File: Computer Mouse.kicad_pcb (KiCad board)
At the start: 2 copper layers, 86 parts, among them J1 Conn_01x05, J2 USB_C_Receptacle_USB2.0, J3 Conn_01x02, SW1 SW_SPST, SW2 SW_SPDT, SW3 SW_SPDT, SW4 RotaryEncoder, SW5 SW_SPDT, SW6 SW_SPDT, SW7 RotaryEncoder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

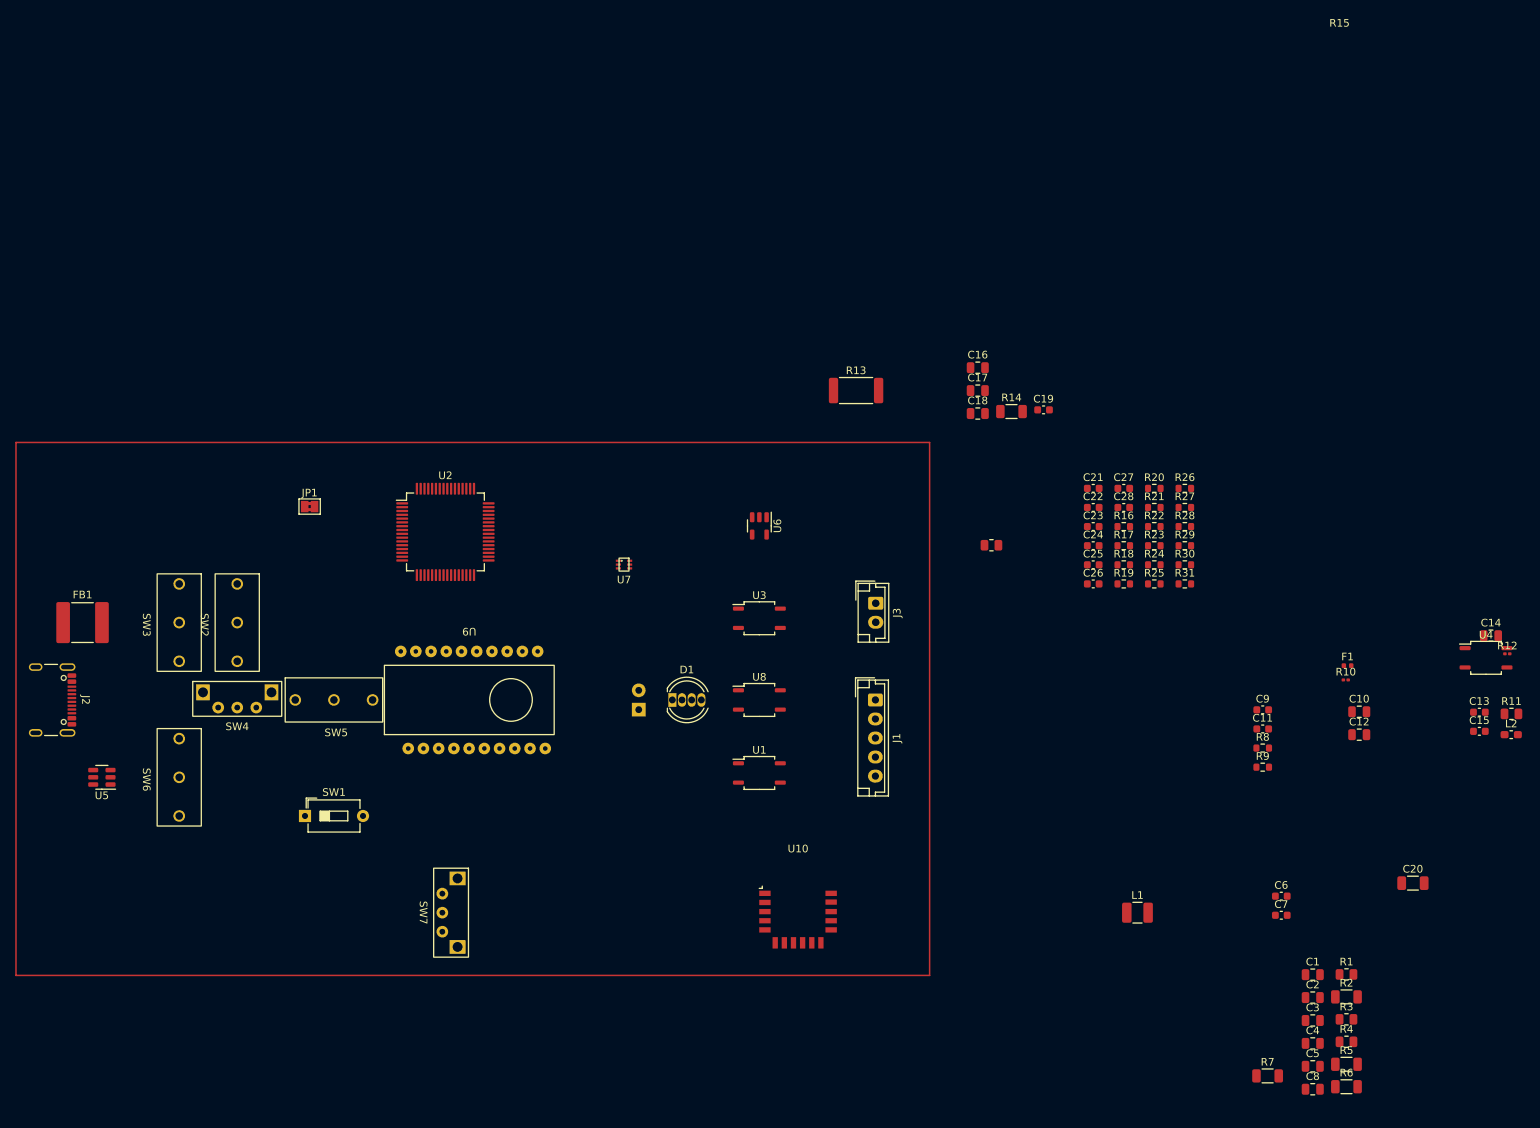
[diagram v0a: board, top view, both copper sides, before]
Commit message: Arrangement of elements
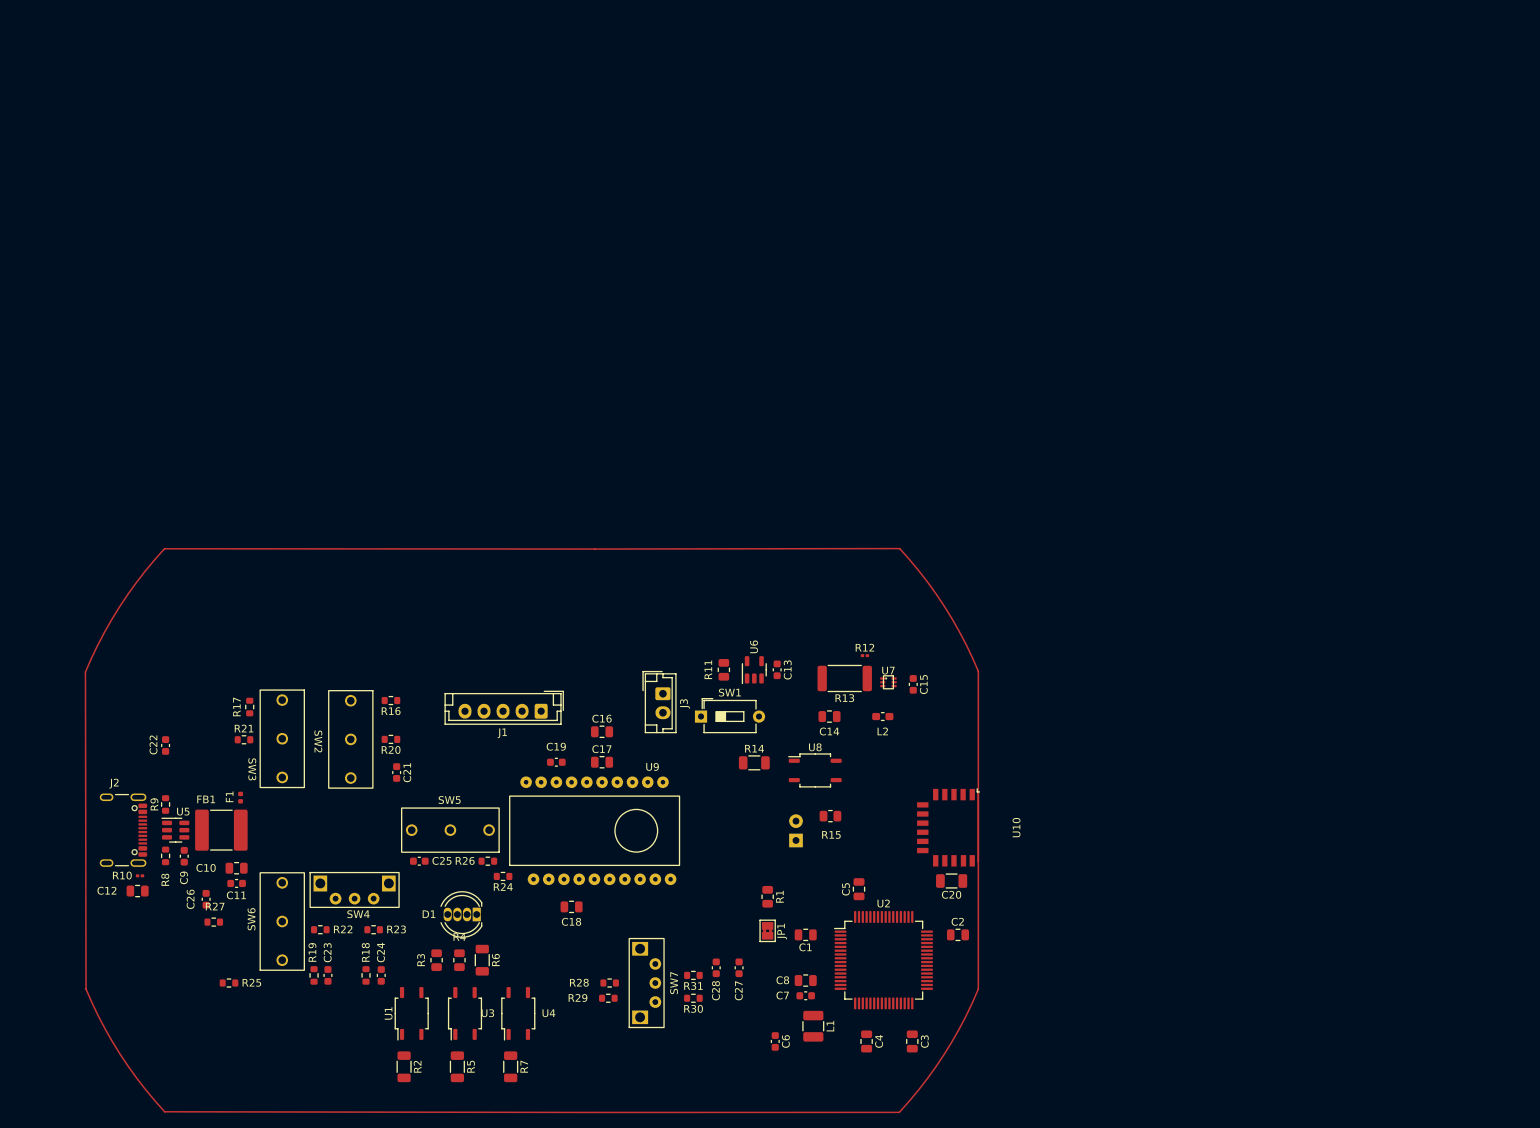
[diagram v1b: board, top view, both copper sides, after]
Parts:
- moved C12 161.8 mm to (86.0, 108.9), turned to 180 degrees
- moved R10 160.4 mm to (86.3, 106.9), turned to 180 degrees
- moved C10 148.9 mm to (99.0, 105.9)
- moved F1 146.4 mm to (99.5, 96.7), turned to -90 degrees
- moved R8 144.8 mm to (89.7, 104.3), turned to -90 degrees
- moved R9 144.2 mm to (89.7, 97.5), turned to 90 degrees
- moved C9 142.9 mm to (92.1, 104.3), turned to 90 degrees
- moved R27 138.7 mm to (96.0, 113.0)
- moved C11 136.3 mm to (99.0, 107.9)
- moved U4 135.4 mm to (136.0, 125.0), turned to 90 degrees
- moved R25 132.4 mm to (98.0, 121.0), turned to 180 degrees
- moved C22 125.8 mm to (89.7, 89.8), turned to -90 degrees
- moved R2 124.1 mm to (121.0, 132.0), turned to -90 degrees
- moved C26 123.7 mm to (95.0, 110.0), turned to 90 degrees
- moved R21 123.4 mm to (100.0, 89.0)
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
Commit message: Board outlines
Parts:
- D2: moved to F.Cu
- moved R15 3.12 mm to (176.8, 102.2)
- moved D2 2.56 mm to (172.3, 99.7), turned to -90 degrees
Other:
- board outline added: 117.3 x 74.1 mm

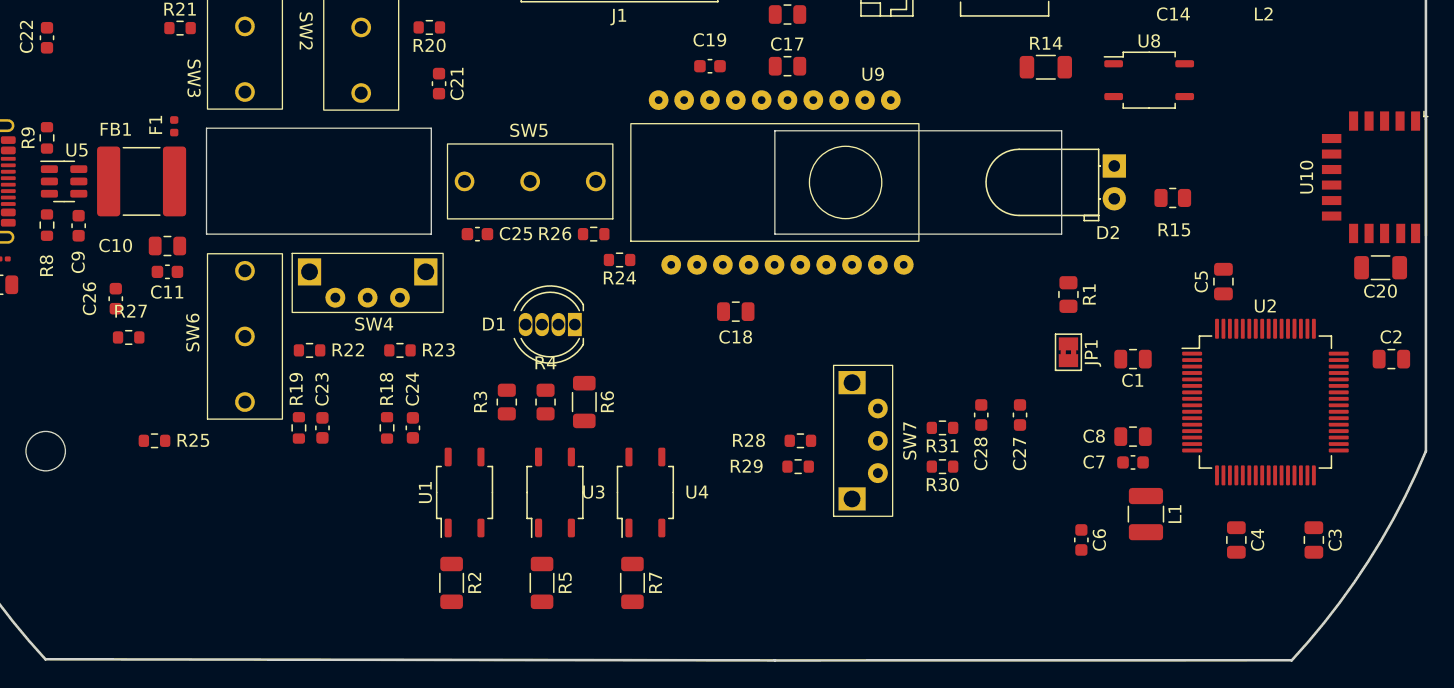
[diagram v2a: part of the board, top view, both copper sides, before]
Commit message: MCU-BT connection
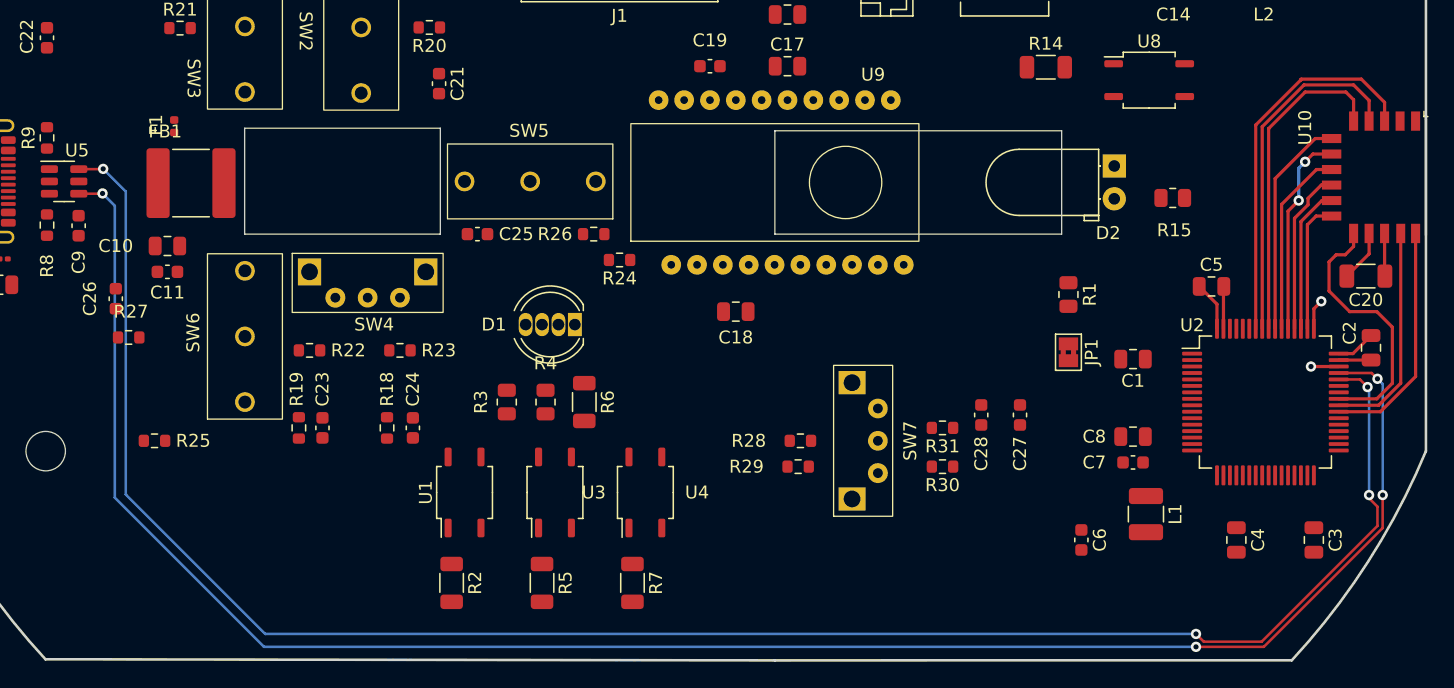
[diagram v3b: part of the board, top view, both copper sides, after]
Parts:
- moved FB1 3.83 mm to (100.8, 101.0)
- moved C2 1.80 mm to (192.2, 113.8), turned to -90 degrees
- moved C20 1.31 mm to (191.8, 108.2)
- moved C5 1.00 mm to (179.8, 109.0), turned to 0 degrees
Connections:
- R2 pad 2: Net-(U2-PA15) -> unconnected-(R2-Pad2)
- R5 pad 2: Net-(U2-PB3) -> unconnected-(R5-Pad2)
- R7 pad 2: Net-(U2-PA2) -> unconnected-(R7-Pad2)
- U2 pad 16: Net-(U2-PA2) -> unconnected-(U2-PA2-Pad16)
- U2 pad 2: BT_P0_0 -> unconnected-(U2-PC13-Pad2)
- U2 pad 29: BT_P2_0 -> unconnected-(U2-PB10-Pad29)
- U2 pad 3: BT_P3_6 -> unconnected-(U2-PC14-Pad3)
- U2 pad 30: BT_P1_2 -> unconnected-(U2-PB11-Pad30)
- U2 pad 33: BT_P1_3 -> unconnected-(U2-PB12-Pad33)
- U2 pad 34: BT_P1_6 -> unconnected-(U2-PB13-Pad34)
- U2 pad 35: BT_P1_7 -> unconnected-(U2-PB14-Pad35)
- U2 pad 36: BT_P0_2 -> unconnected-(U2-PB15-Pad36)
- U2 pad 37: SW7A -> unconnected-(U2-PC6-Pad37)
- U2 pad 38: SW7B -> unconnected-(U2-PC7-Pad38)
- U2 pad 39: unconnected-(U2-PC8-Pad39) -> BT_P2_0
- U2 pad 4: BT_P2_7 -> unconnected-(U2-PC15-Pad4)
- U2 pad 40: unconnected-(U2-PC9-Pad40) -> BT_P2_7
- U2 pad 41: MOTION -> BT_P0_2
- U2 pad 50: Net-(U2-PA15) -> BT_P0_0
- U2 pad 51: BT_RX -> BT_RST
- U2 pad 52: BT_TX -> BT_P3_6
- U2 pad 53: BT_RST -> BT_RX
- U2 pad 54: unconnected-(U2-PD2-Pad54) -> BT_TX
- U2 pad 55: Net-(U2-PB3) -> BT_P1_6
- U2 pad 56: unconnected-(U2-PB4-Pad56) -> BT_P1_7
- U2 pad 57: unconnected-(U2-PB5-Pad57) -> BT_P1_3
- U2 pad 58: unconnected-(U2-PB6-Pad58) -> BT_P1_2
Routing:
- net D+: track 0.00 -> 147.4 mm, vias 0 -> 4
- net D-: track 0.00 -> 146.7 mm, vias 0 -> 4
- net BT_P1_2: track 0.00 -> 29.4 mm
- net BT_P1_3: track 0.00 -> 27.3 mm
- net BT_P1_7: track 0.00 -> 25.1 mm
- net BT_P0_2: track 0.00 -> 20.7 mm
- net BT_P2_0: track 0.00 -> 18.2 mm
- net BT_P1_6: track 0.00 -> 17.3 mm
- net BT_P2_7: track 0.00 -> 17.1 mm
- net BT_RX: track 0.00 -> 15.8 mm, vias 0 -> 2
- net BT_TX: track 0.00 -> 14.6 mm
- net BT_P3_6: track 0.00 -> 12.8 mm
- net BT_RST: track 0.00 -> 11.3 mm
- net +3V3: track 0.00 -> 10.2 mm
- net BT_P0_0: track 0.00 -> 10.2 mm
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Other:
- outline, holes or cut-outs redrawn

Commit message: Other connections
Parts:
- moved C22 10.1 mm to (99.2, 93.2)
- moved C16 9.87 mm to (138.0, 92.1)
- moved C17 9.21 mm to (138.0, 90.0)
- moved R18 7.58 mm to (118.3, 112.8)
- moved R19 7.23 mm to (110.2, 112.8)
- moved C15 5.80 mm to (184.9, 76.8), turned to 90 degrees
- moved C27 5.78 mm to (161.3, 123.5), turned to 0 degrees
- moved R12 5.55 mm to (181.3, 83.5)
- moved U7 5.18 mm to (181.3, 85.5)
- moved R26 4.90 mm to (127.1, 105.5), turned to 90 degrees
- moved C6 4.81 mm to (174.3, 130.0)
- moved R27 4.28 mm to (100.2, 112.9)
- moved C13 4.08 mm to (170.9, 75.9), turned to 90 degrees
- moved C24 4.04 mm to (116.6, 116.2)
- moved C23 3.87 mm to (112.0, 116.2)
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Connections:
- C7 pad 2: Net-(C7-Pad2) -> GND
- C8 pad 2: Net-(C7-Pad2) -> GND
- R2 pad 2: unconnected-(R2-Pad2) -> Net-(U2-PA2)
- R5 pad 2: unconnected-(R5-Pad2) -> Net-(U2-PA1)
- R7 pad 2: unconnected-(R7-Pad2) -> Net-(U2-PA0)
- U2 pad 10: SW5 -> SW2
- U2 pad 11: SW6 -> SW3
- U2 pad 14: +BATT -> Net-(U2-PA0)
- U2 pad 15: REF -> Net-(U2-PA1)
- U2 pad 16: unconnected-(U2-PA2-Pad16) -> Net-(U2-PA2)
- U2 pad 17: STAT -> unconnected-(U2-PA3-Pad17)
- U2 pad 24: SW4A -> SW7B
- U2 pad 25: SW4B -> SW7A
- U2 pad 26: unconnected-(U2-PB0-Pad26) -> SW5
- U2 pad 27: unconnected-(U2-PB1-Pad27) -> SW4B
- U2 pad 28: unconnected-(U2-PB2-Pad28) -> SW4A
- U2 pad 29: unconnected-(U2-PB10-Pad29) -> SW6
- U2 pad 59: unconnected-(U2-PB7-Pad59) -> STAT
- U2 pad 61: unconnected-(U2-PB8-Pad61) -> MOTION
- U2 pad 8: SW2 -> +BATT
- U2 pad 9: SW3 -> REF
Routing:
- net SW3: track 0.00 -> 168.4 mm, vias 0 -> 2
- net GND: track 9.80 -> 135.4 mm
- net SW6: track 0.00 -> 114.3 mm
- net +5V: track 0.00 -> 111.2 mm
- net SW4A: track 0.00 -> 103.3 mm
- net SW4B: track 0.00 -> 98.4 mm
- net SW5: track 0.00 -> 87.4 mm
- net SW2: track 0.00 -> 80.1 mm
- net NRST: track 0.00 -> 79.7 mm, vias 0 -> 1
- net SCLK: track 0.00 -> 75.5 mm, vias 0 -> 2
- net SWCLK: track 2.15 -> 75.3 mm
- net +BATT: track 0.00 -> 70.2 mm, vias 0 -> 2
- net Net-(U2-PA2): track 0.00 -> 68.3 mm, vias 0 -> 2
- net SWDIO: track 2.36 -> 67.6 mm
- net Net-(U2-PA1): track 0.00 -> 57.5 mm, vias 0 -> 2
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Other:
- outline, holes or cut-outs redrawn

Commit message: Bugfixes
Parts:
- D1: footprint LED_THT:LED_D5.0mm-4_RGB -> LED_THT:LED_D5.0mm-4_RGB_Wide_Pins
- R10: footprint Resistor_SMD:R_0201_0603Metric -> Resistor_SMD:R_1206_3216Metric
- R12: footprint Resistor_SMD:R_0201_0603Metric -> Resistor_SMD:R_0805_2012Metric
- R13: footprint Resistor_SMD:R_2512_6332Metric -> Resistor_SMD:R_0805_2012Metric
- SW1: moved to B.Cu
- moved R6 4.30 mm to (135.1, 118.5)
- moved R10 4.28 mm to (87.2, 111.2)
- moved R3 4.20 mm to (121.0, 117.8)
- moved C15 3.87 mm to (182.2, 79.5)
- moved R7 1.98 mm to (136.3, 130.5), turned to 0 degrees
- moved R2 1.98 mm to (122.4, 130.6), turned to 0 degrees
- moved R5 1.91 mm to (129.3, 130.6), turned to 0 degrees
- moved R4 1.55 mm to (126.5, 117.8)
- moved R12 1.05 mm to (181.2, 82.5)
- moved R13 0.81 mm to (180.3, 79.4)
- moved C12 0.67 mm to (86.8, 108.3)
- moved D1 0.34 mm to (130.8, 112.2)
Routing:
- net Net-(J2-SHIELD): track 3.72 -> 23.0 mm
- net +3V3: track 60.8 -> 55.4 mm
- net D+: track 147.0 -> 142.0 mm
- net D-: track 145.6 -> 140.8 mm
- net Net-(U2-PA2): track 68.3 -> 63.5 mm
- net Net-(U2-PA1): track 57.5 -> 53.1 mm
- net Net-(U2-PA0): track 48.7 -> 44.6 mm
- net GND: track 135.4 -> 131.6 mm
- net Net-(R6-Pad2): track 6.03 -> 2.65 mm
- net SW4B: track 98.4 -> 95.1 mm
- net Net-(D1-BK): track 5.71 -> 8.96 mm
- net Net-(R3-Pad1): track 6.43 -> 3.80 mm
- net SW5: track 87.4 -> 85.2 mm
- net Net-(C10-Pad2): track 14.1 -> 12.4 mm
- net SW6: track 114.3 -> 112.8 mm
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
